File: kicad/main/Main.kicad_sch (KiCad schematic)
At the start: 0 parts

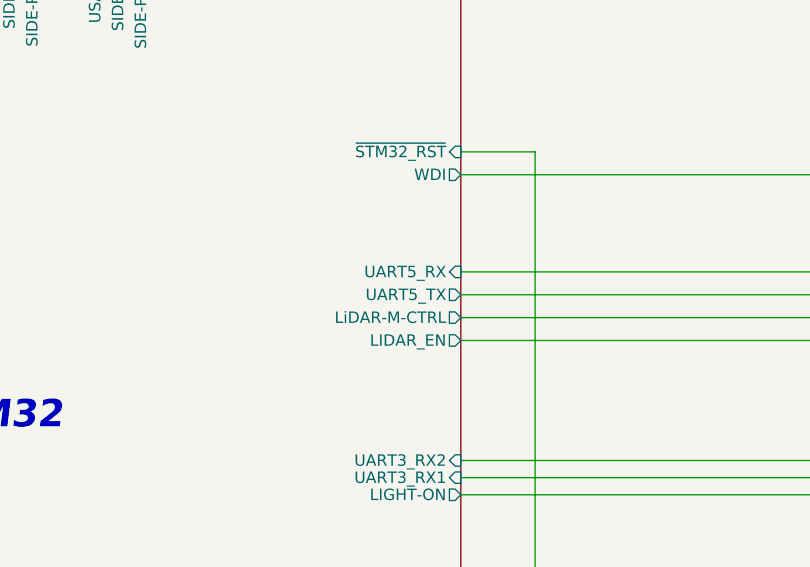
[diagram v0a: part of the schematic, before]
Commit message: Add main-phone: v1 board with a smartphone as the compute
kicad/main-phone is a fork of the Pi carrier for the first board: an
Android phone talks to the STM32 over USB-C, no Pi, cameras, M.2, SD,
speaker or mopping. The Pi board (kicad/main) stays in the plans.

v1 board:
- USB-C CC1/CC2 to the STM32 UCPD; reverse-block FETs for the TMI6240
- front ToF on I2C4; LiDAR UART TX/RX unswapped
- power control: charger rail-hold, ~4-9 s hardware off timer
- 20 V input: SMAJ22A TVS, 50 V DC_IN caps, DC_IN sense to PB15
- low-profile DC-044A-20A barrel jack (footprint + 3D model added)
- on-board ITR9606 bumpers in parallel with the harness bumpers
- carpet drive AC-coupled; right-angle 1x5 for LiDAR and debug headers
- spare I/O pads (2x6), pull-up/series fixes, BOM consolidation

Also: README and SPEC updated (v1 sections, STM32G473), LiDAR UART
net names on the Pi board.

Co-Authored-By: Claude Opus 5.5 (1M context) <noreply@anthropic.com>
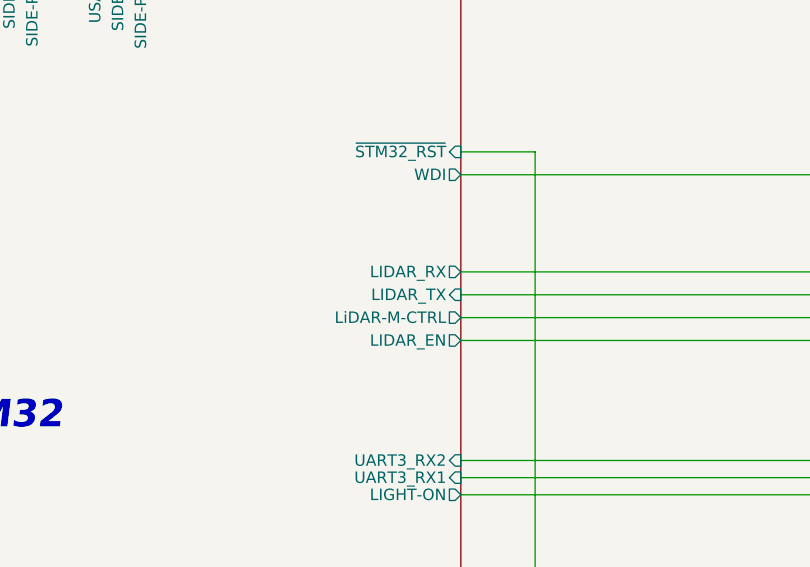
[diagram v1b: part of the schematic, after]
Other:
- sheet MCU-STM32 ports: added LIDAR_RX, LIDAR_TX; removed UART5_RX, UART5_TX
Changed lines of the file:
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@@
 			)
 		)
-		(pin "UART5_RX" input
+		(pin "LIDAR_RX" output
 			(at 266.7 157.48 0)
 			(effects
@@
 			)
 		)
-		(pin "UART5_TX" output
+		(pin "LIDAR_TX" input
 			(at 266.7 160.02 0)
 			(effects
